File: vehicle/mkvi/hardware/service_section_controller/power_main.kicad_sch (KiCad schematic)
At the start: 32 parts

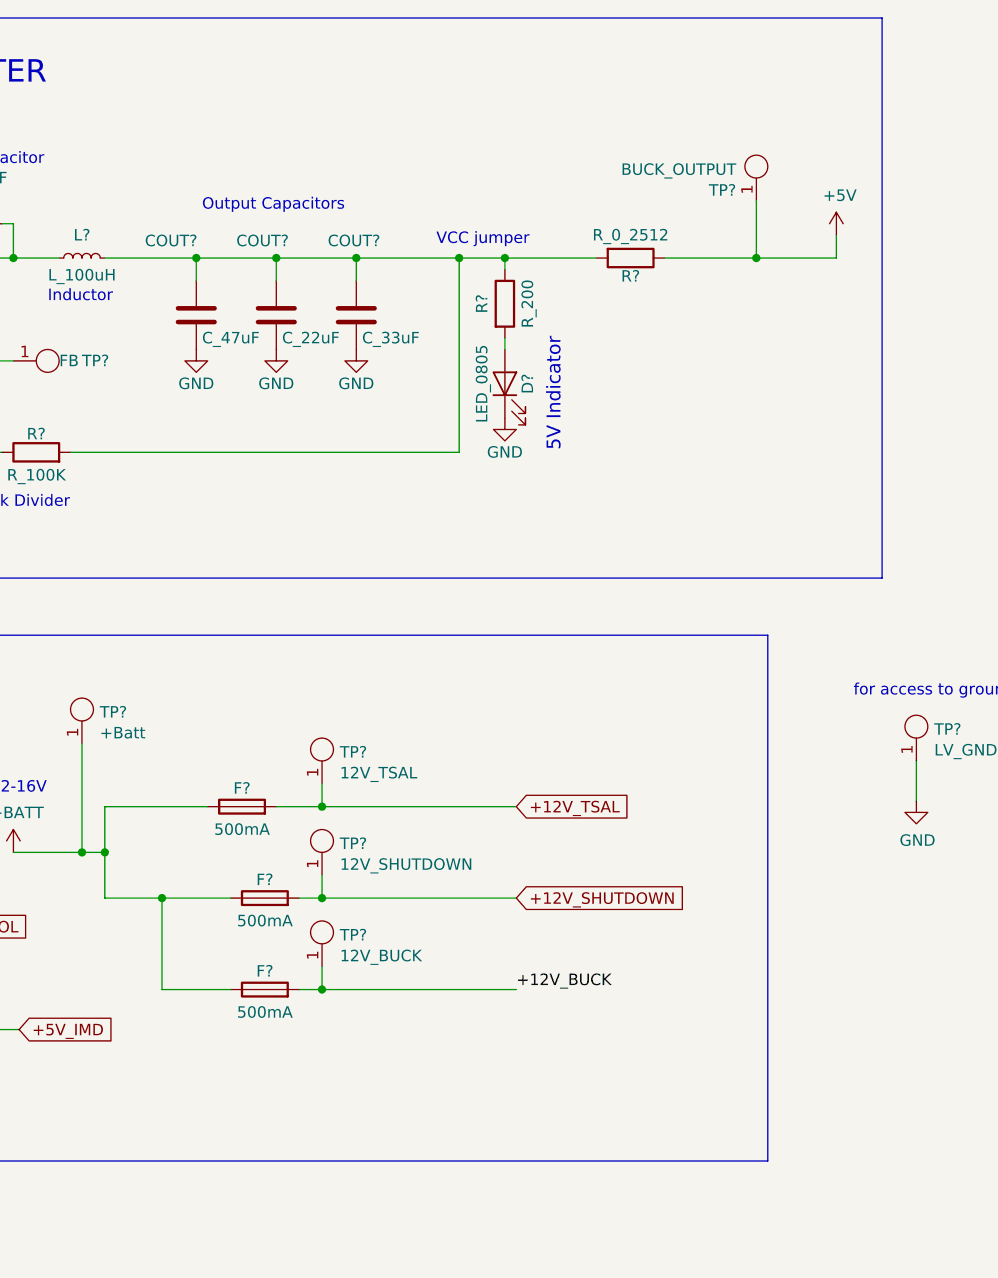
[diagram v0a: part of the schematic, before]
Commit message: schematic finished
made edits to schematic according to comments :)
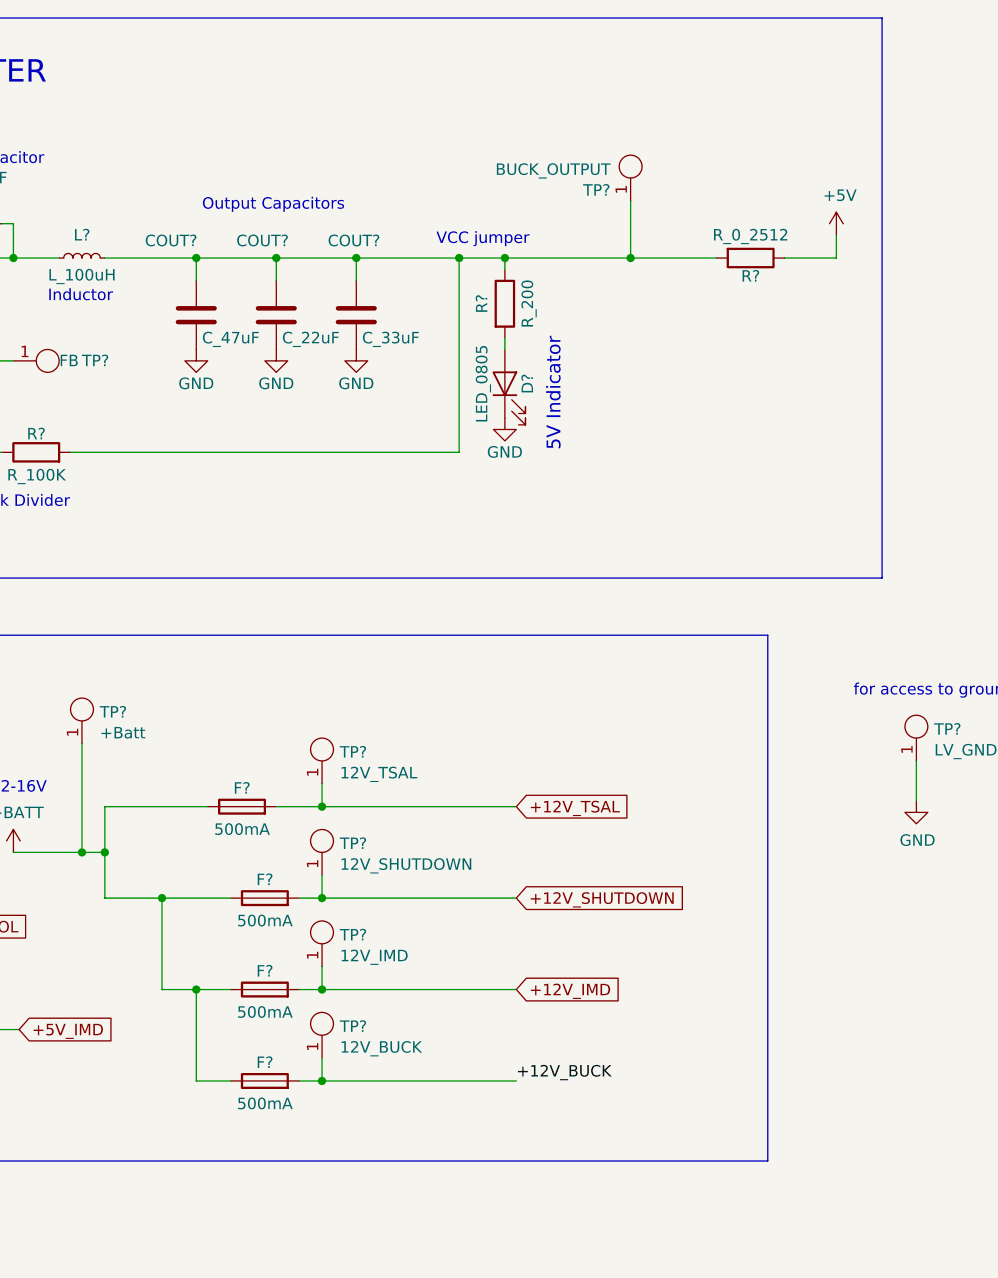
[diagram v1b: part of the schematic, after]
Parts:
- added F?: 500mA, footprints:Fuse_1210, symbol formula:F_500mA_16V
- added TP?: 12V_BUCK, TestPoint:TestPoint_Pad_D1.0mm, symbol formula:Test_Point_SMD
- TP?: value 12V_BUCK -> 12V_IMD
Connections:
- net +12V_BUCK: now also F?.2, TP?.1; no longer F?.2, TP?.1
- net +5V: no longer TP?.1
- net +BATT: now also F?.1
- net at COUT?.1, COUT?.1, COUT?.1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: now also TP?.1
- new net +12V_IMD: F?.2, TP?.1
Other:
- moved on the sheet: R?, TP?

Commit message: beginning layout changes
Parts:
- gave numbers to parts that had none: 34
